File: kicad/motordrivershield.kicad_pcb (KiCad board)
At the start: 2 copper layers, 100 x 60 mm, 155 parts, among them CN1 ARDUINO_MKR, CN2 QWIIC, CN3 ARDUINO_NANO_33, P1 CONN_01X03, P2 CONN_01X03, P5 WR-TBL_691313710002, P6 WR-TBL_691313710002, P7 CONN_01X02, P8 WR-TBL_691313710002, Q1 2N7002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

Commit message: bom update
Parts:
- C15, C17, C21: value 47 uF -> 47uF
- C3, C4: value 22 uF -> 22uF
- C35, C36: value 1n -> 1nF
- C5: value 100 nF -> 100nF
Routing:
- net GND: vias 199 -> 197

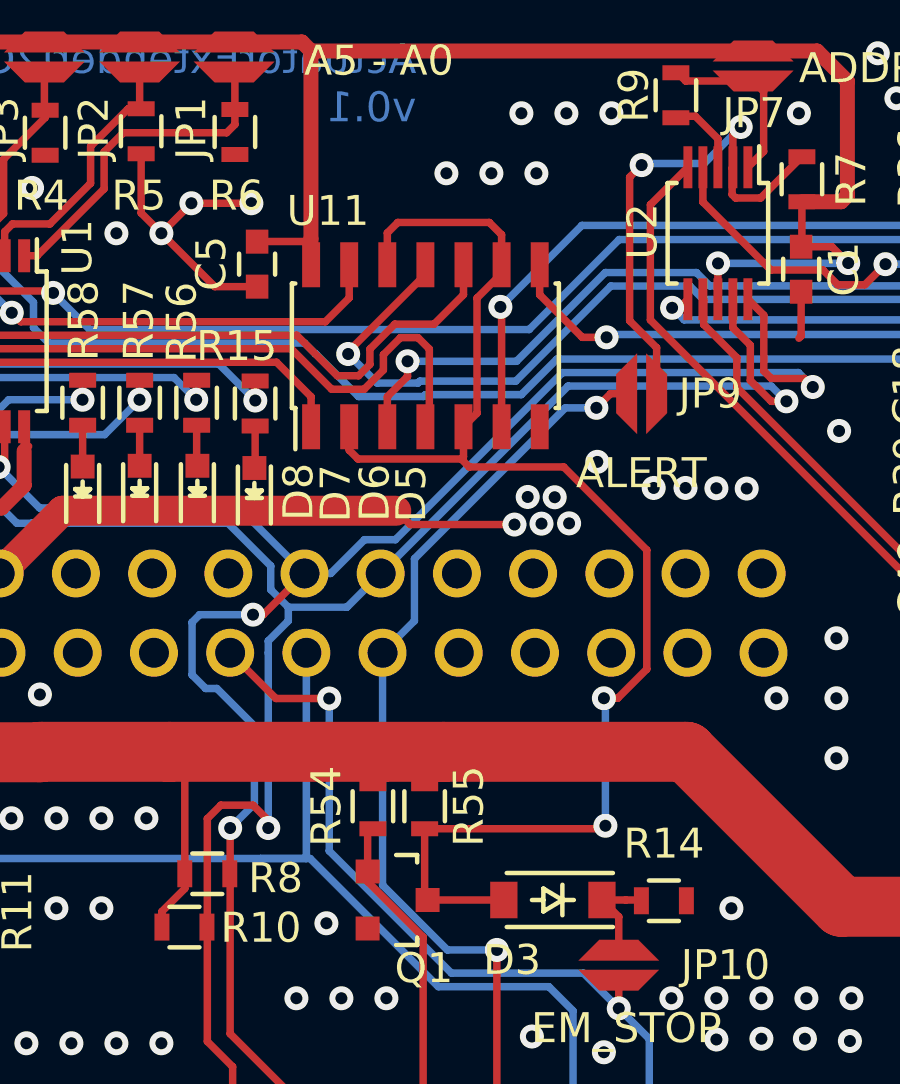
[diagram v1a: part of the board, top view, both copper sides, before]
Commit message: improved emergency stop for breaking
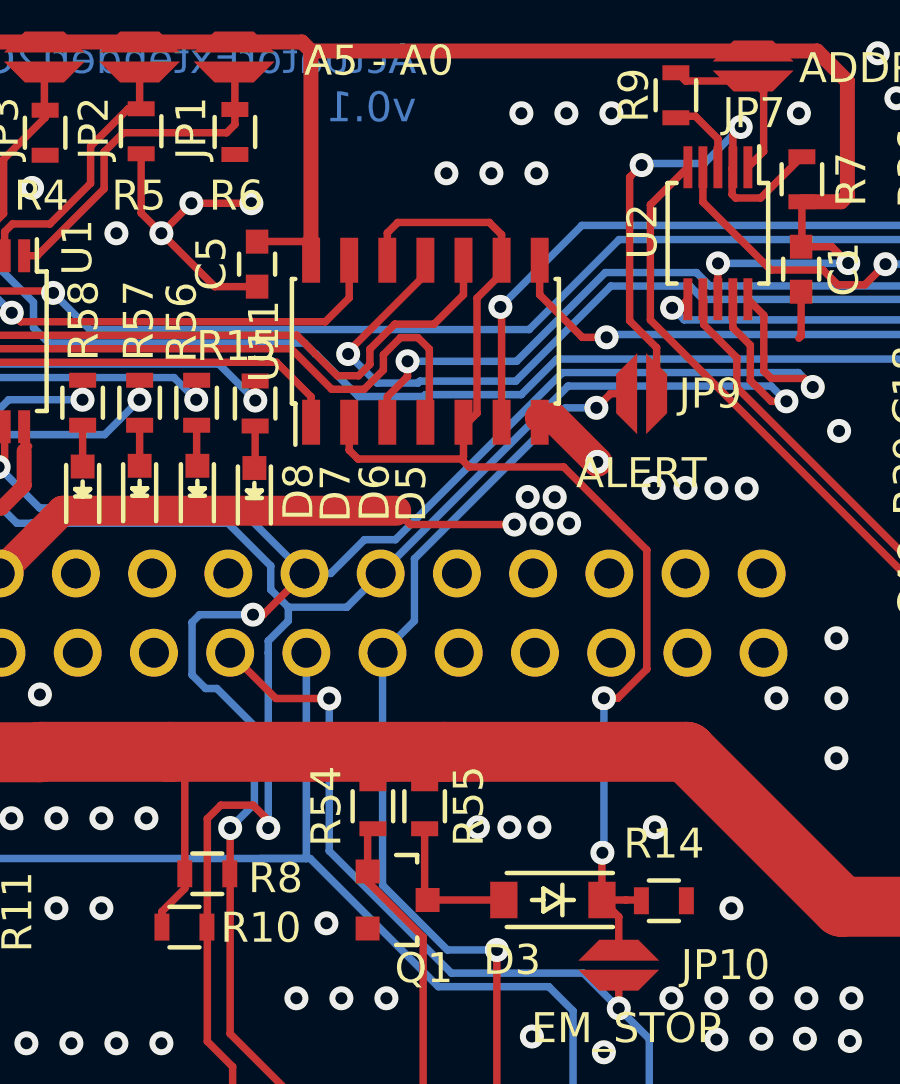
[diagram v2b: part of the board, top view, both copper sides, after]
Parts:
- U11: value 74xx08 -> 74xx32
- moved U11 0.15 mm to (120.3, 52.1)
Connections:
- U11 pad 12: /powertrain/EM_S -> EM_STOP
- U11 pad 2: /powertrain/EM_S -> EM_STOP
- U11 pad 5: /powertrain/EM_S -> EM_STOP
- U11 pad 9: /powertrain/EM_S -> EM_STOP
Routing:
- net /powertrain/EM_S: track 46.9 -> 5.44 mm, vias 2 -> 0
- net EM_STOP: track 3.23 -> 41.1 mm, vias 0 -> 2
- net GND: track 146.4 -> 148.9 mm, vias 197 -> 201

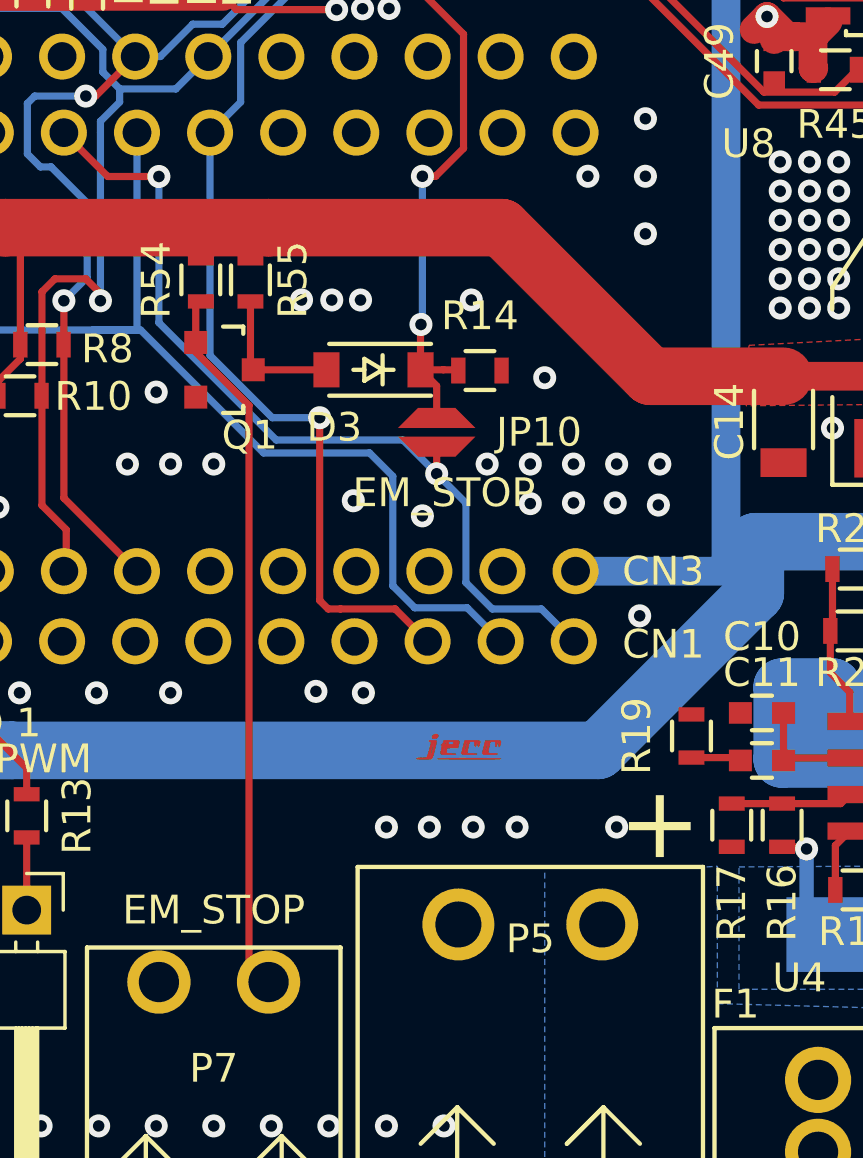
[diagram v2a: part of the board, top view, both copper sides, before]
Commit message: improved emergency stop circuit for breaking
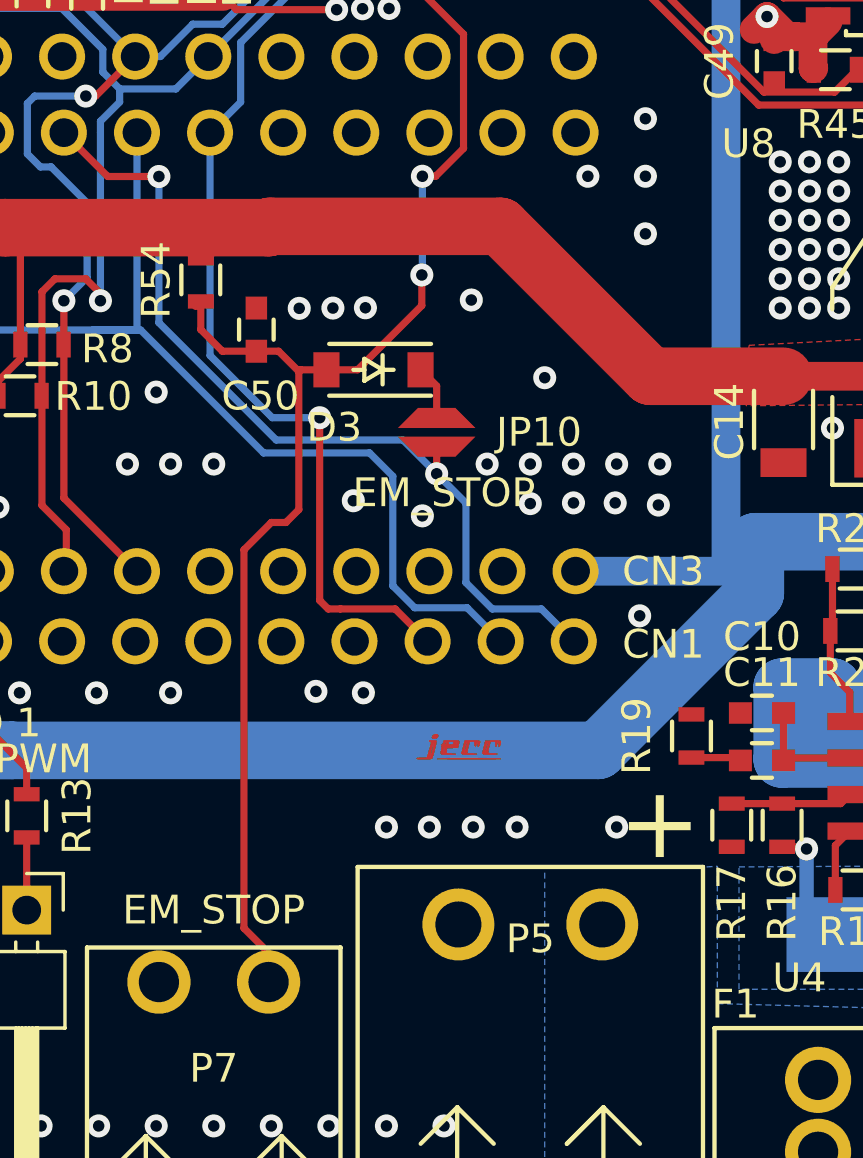
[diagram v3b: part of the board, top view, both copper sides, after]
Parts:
- removed Q1: 2N7002, SOT_TO:SOT-23
- removed R14: 100k, resistors:R_0603
- removed R55: 10k, resistors:R_0603
- added C50: 100nF, capacitors:C_0603, F.Cu at (120.5, 69.3)
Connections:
- P7 pad 2: Net-(P7-Pad2) -> /powertrain/EM_S
- R54 pad 2: Net-(P7-Pad2) -> /powertrain/EM_S
- U11 pad 12: EM_STOP -> /powertrain/EM_S
- U11 pad 2: EM_STOP -> /powertrain/EM_S
- U11 pad 5: EM_STOP -> /powertrain/EM_S
- U11 pad 9: EM_STOP -> /powertrain/EM_S
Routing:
- net /powertrain/EM_S: track 5.44 -> 69.7 mm, vias 0 -> 2
- net EM_STOP: track 41.1 -> 1.91 mm, vias 2 -> 0
- net Net-(P7-Pad2): track 24.8 -> 0.00 mm

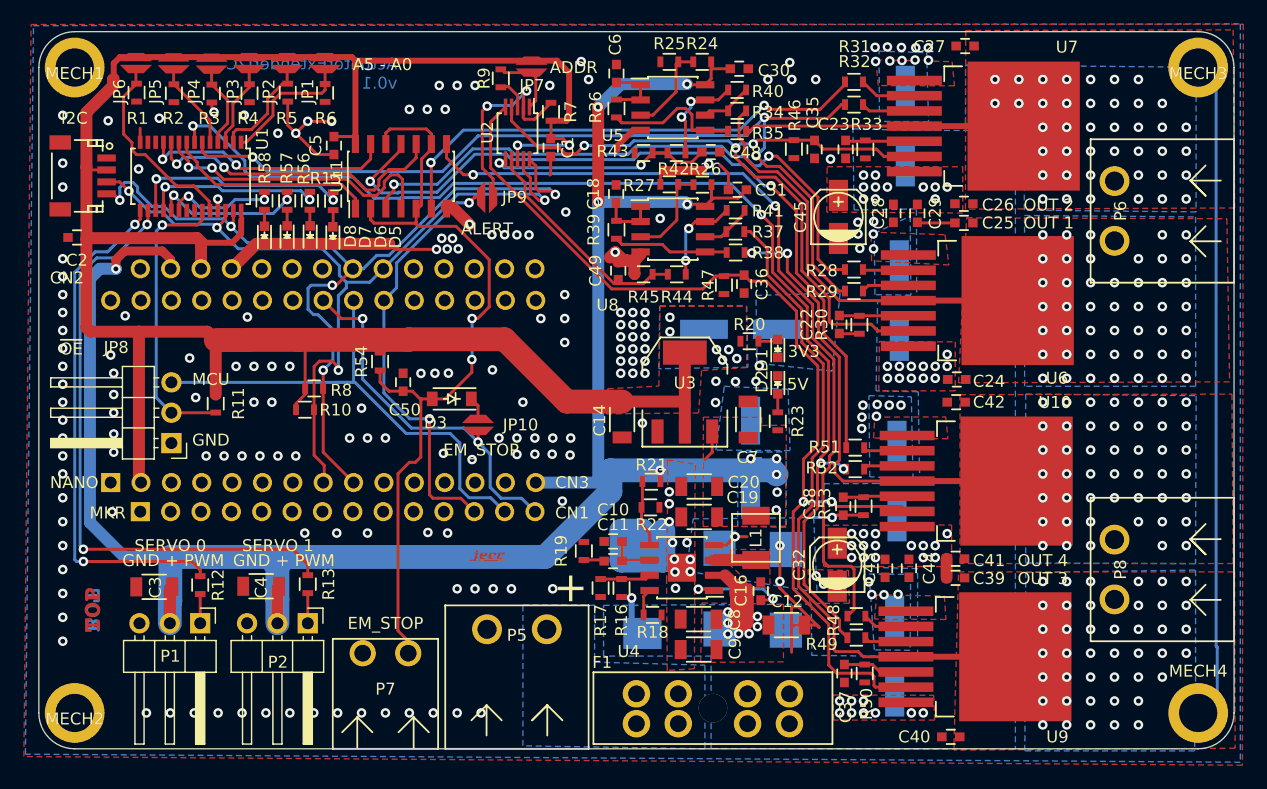
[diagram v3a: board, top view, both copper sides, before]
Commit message: layout improvement
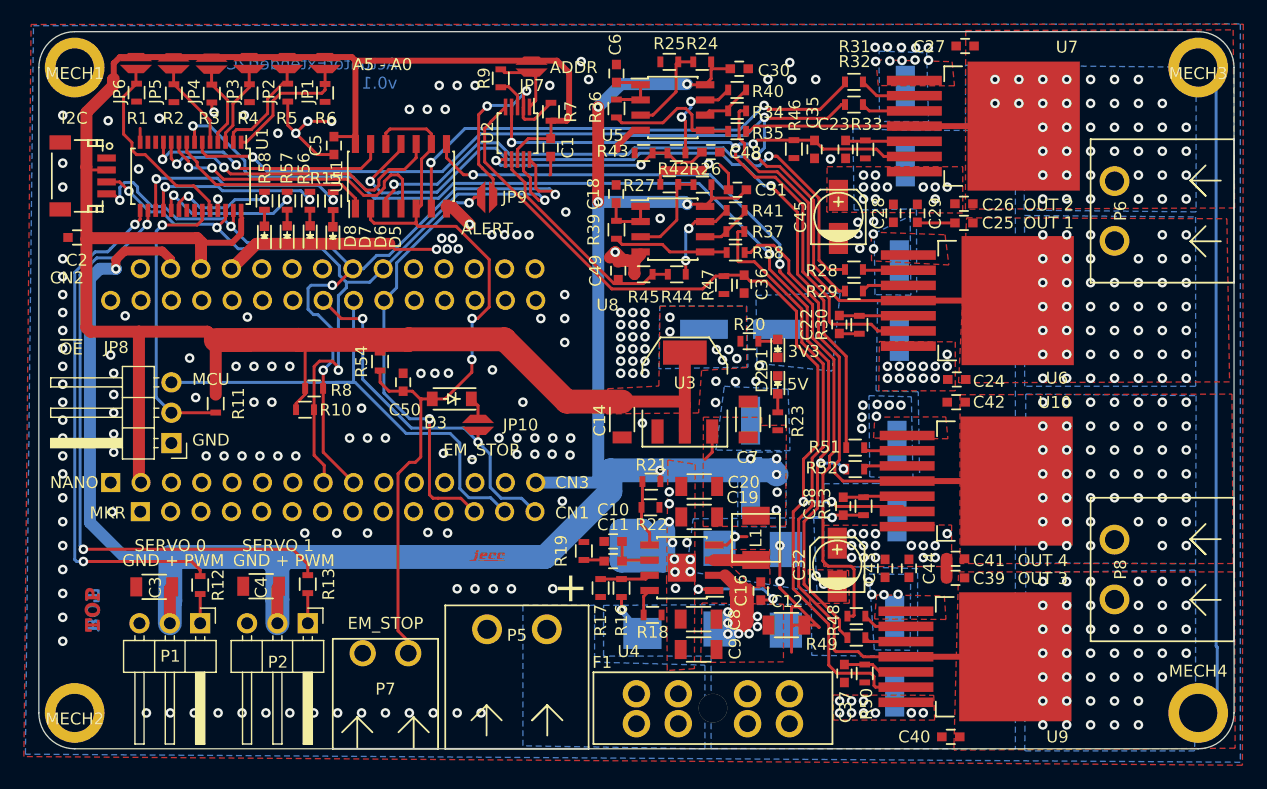
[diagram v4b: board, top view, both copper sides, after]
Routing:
- net +3V3: track 189.7 -> 186.4 mm, vias 8 -> 6
- net INH34: track 96.0 -> 94.5 mm
- net /powertrain/IN3: track 69.4 -> 68.0 mm
- net IS12: track 63.2 -> 64.6 mm
- net /powertrain/OUT3: track 58.2 -> 59.4 mm
- net BEMF12: track 19.0 -> 19.7 mm
- net +BATT: track 12.7 -> 12.2 mm
- net /powertrain/OUT4: track 39.4 -> 39.6 mm, vias 48 -> 46

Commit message: layout improvement
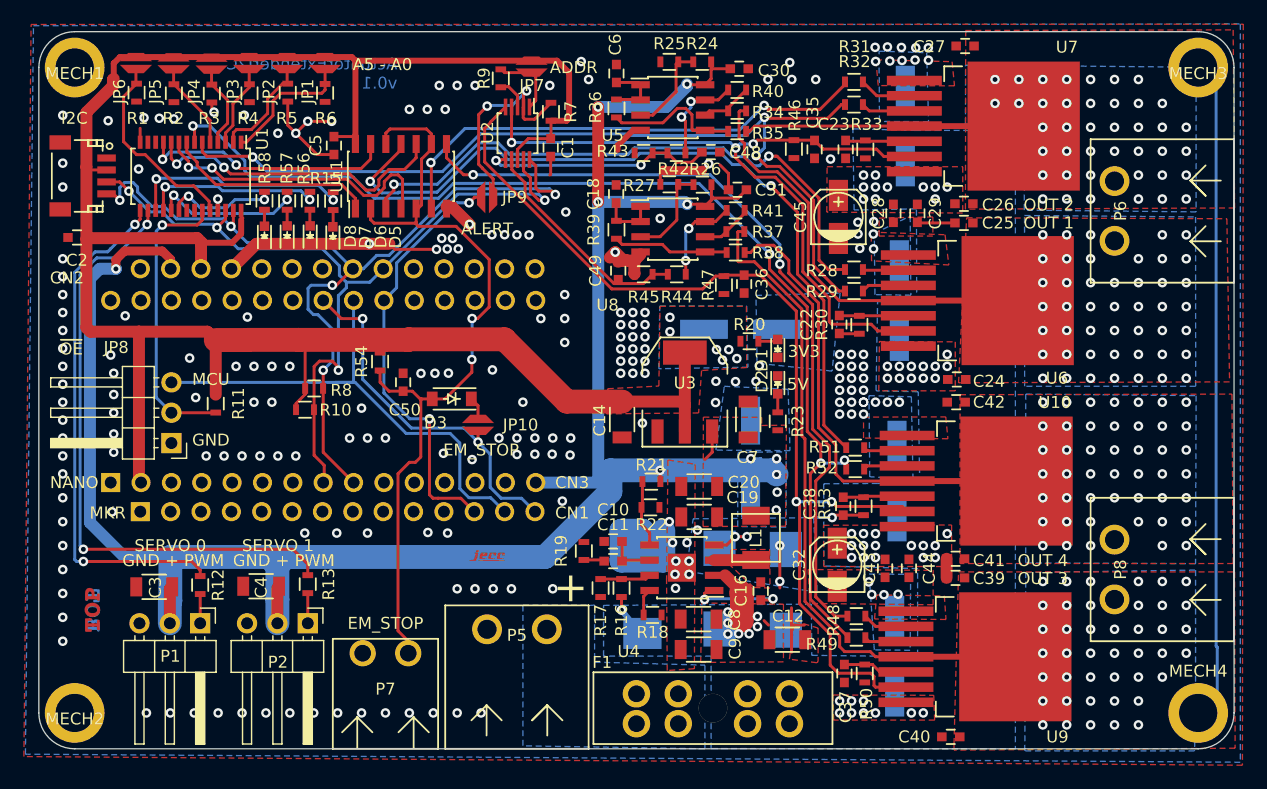
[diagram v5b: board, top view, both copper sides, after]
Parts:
- moved C12 1.22 mm to (152.6, 90.9)
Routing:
- net GND: track 148.9 -> 142.3 mm, vias 201 -> 217
- net /powertrain/OUT3: track 59.4 -> 57.3 mm
- net IS34: track 86.7 -> 85.5 mm
- net /powertrain/IN3: track 68.0 -> 66.9 mm
- net Net-(C16-Pad2): track 9.04 -> 8.21 mm

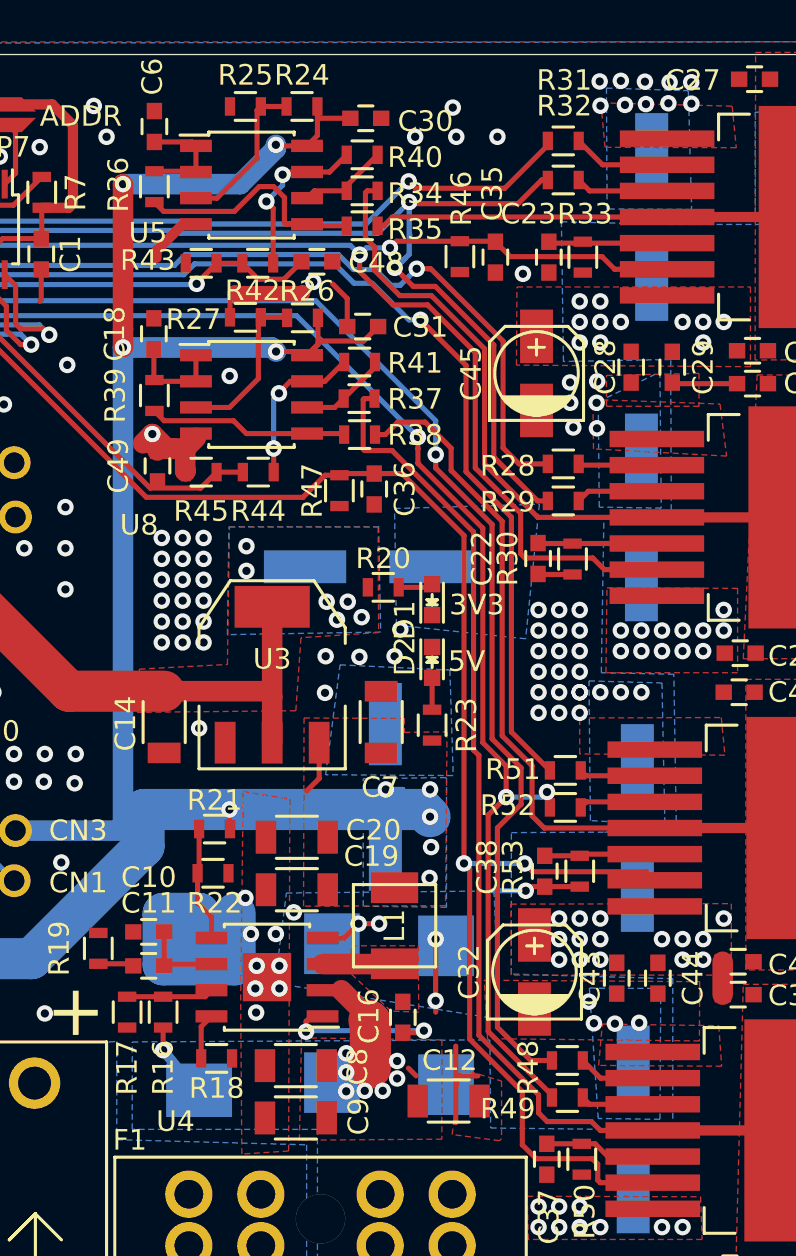
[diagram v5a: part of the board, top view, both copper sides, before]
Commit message: improved ifx ground
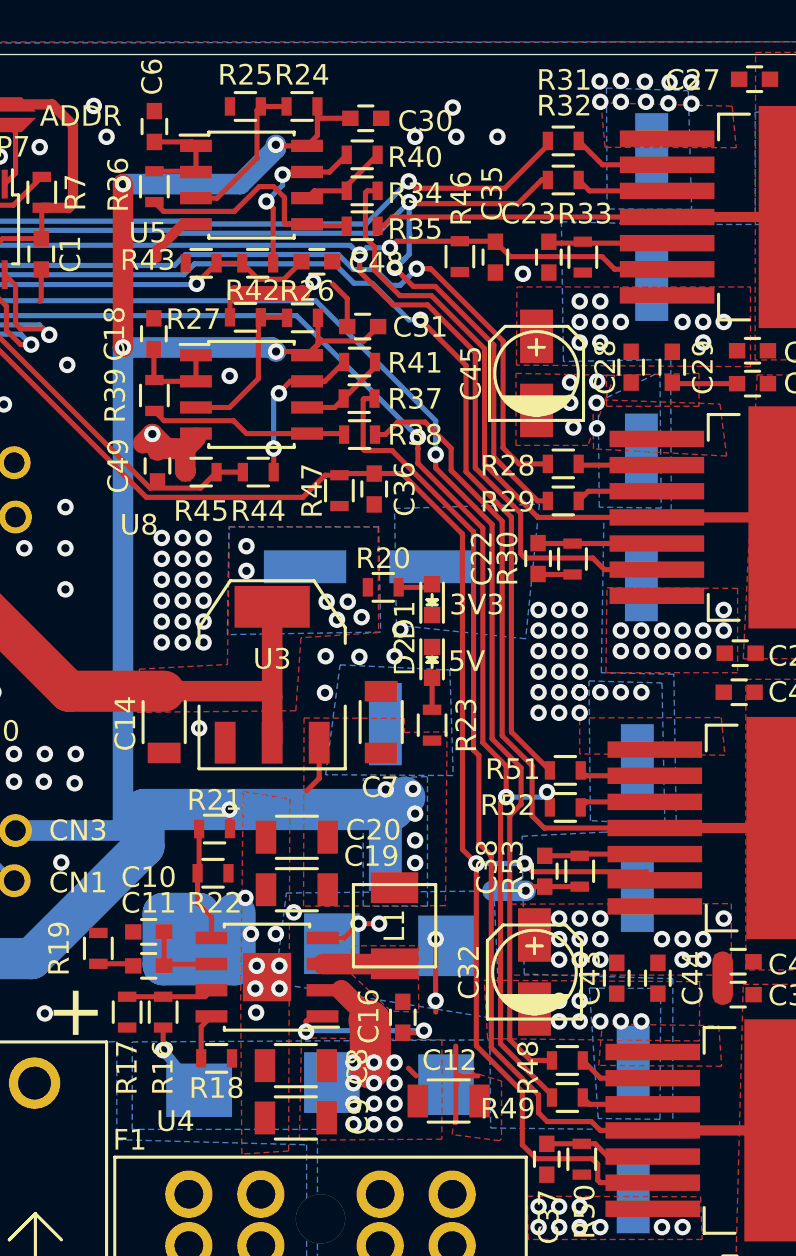
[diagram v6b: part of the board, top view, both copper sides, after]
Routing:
- net +5V: track 197.9 -> 196.8 mm
- net IS34: track 85.5 -> 84.9 mm
- net GND: vias 217 -> 220
- net +BATT: vias 55 -> 60
